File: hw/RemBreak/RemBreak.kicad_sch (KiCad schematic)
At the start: 46 parts, among them IC1 MAX17049G+T10, J1 Conn_01x02, J10 Conn_01x04, J11 Conn_01x01, J3 Conn_01x01, J4 Conn_01x03, J5 Conn_01x02, J6 Conn_01x04, J7 Conn_01x07, J8 Conn_01x03, J9 Conn_01x03, Q1 BC337, Q2 BC337, Q3 BC847, Q4 BC847, U1 L7805, U3 INA219BxDCN, U4 L7805, U5 SeeeduinoXIAO

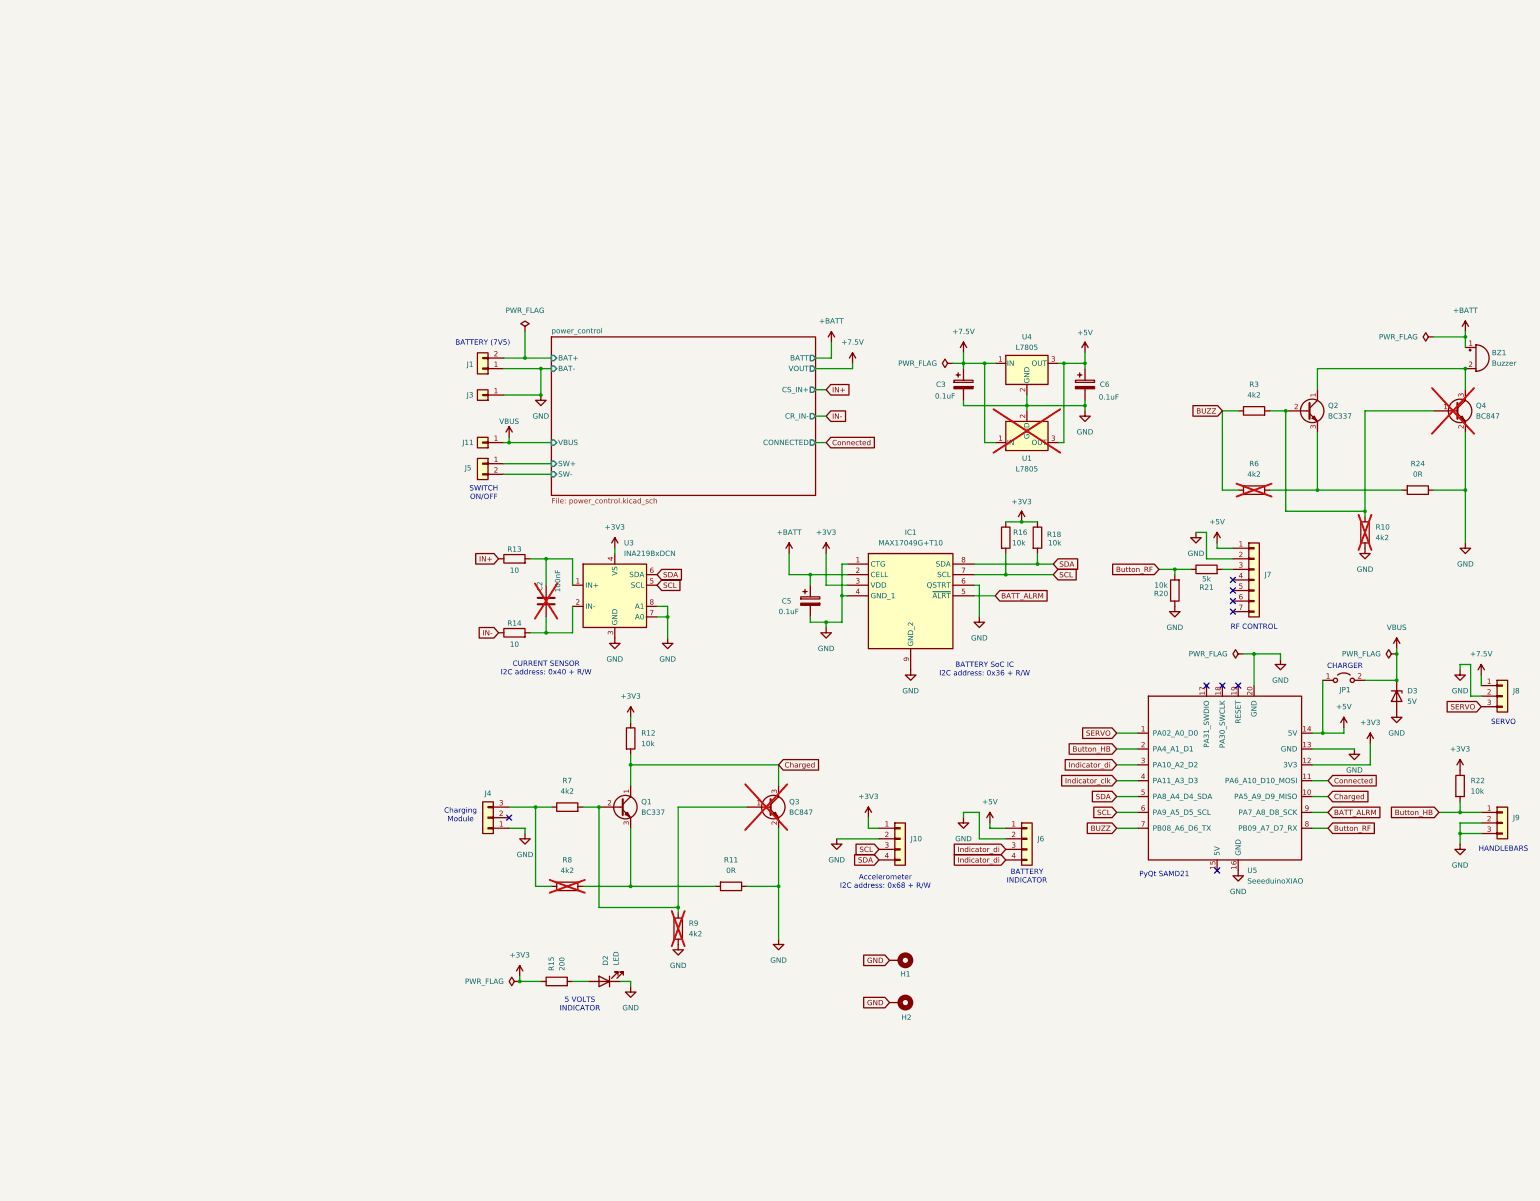
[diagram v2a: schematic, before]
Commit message: updated USBcharger module model
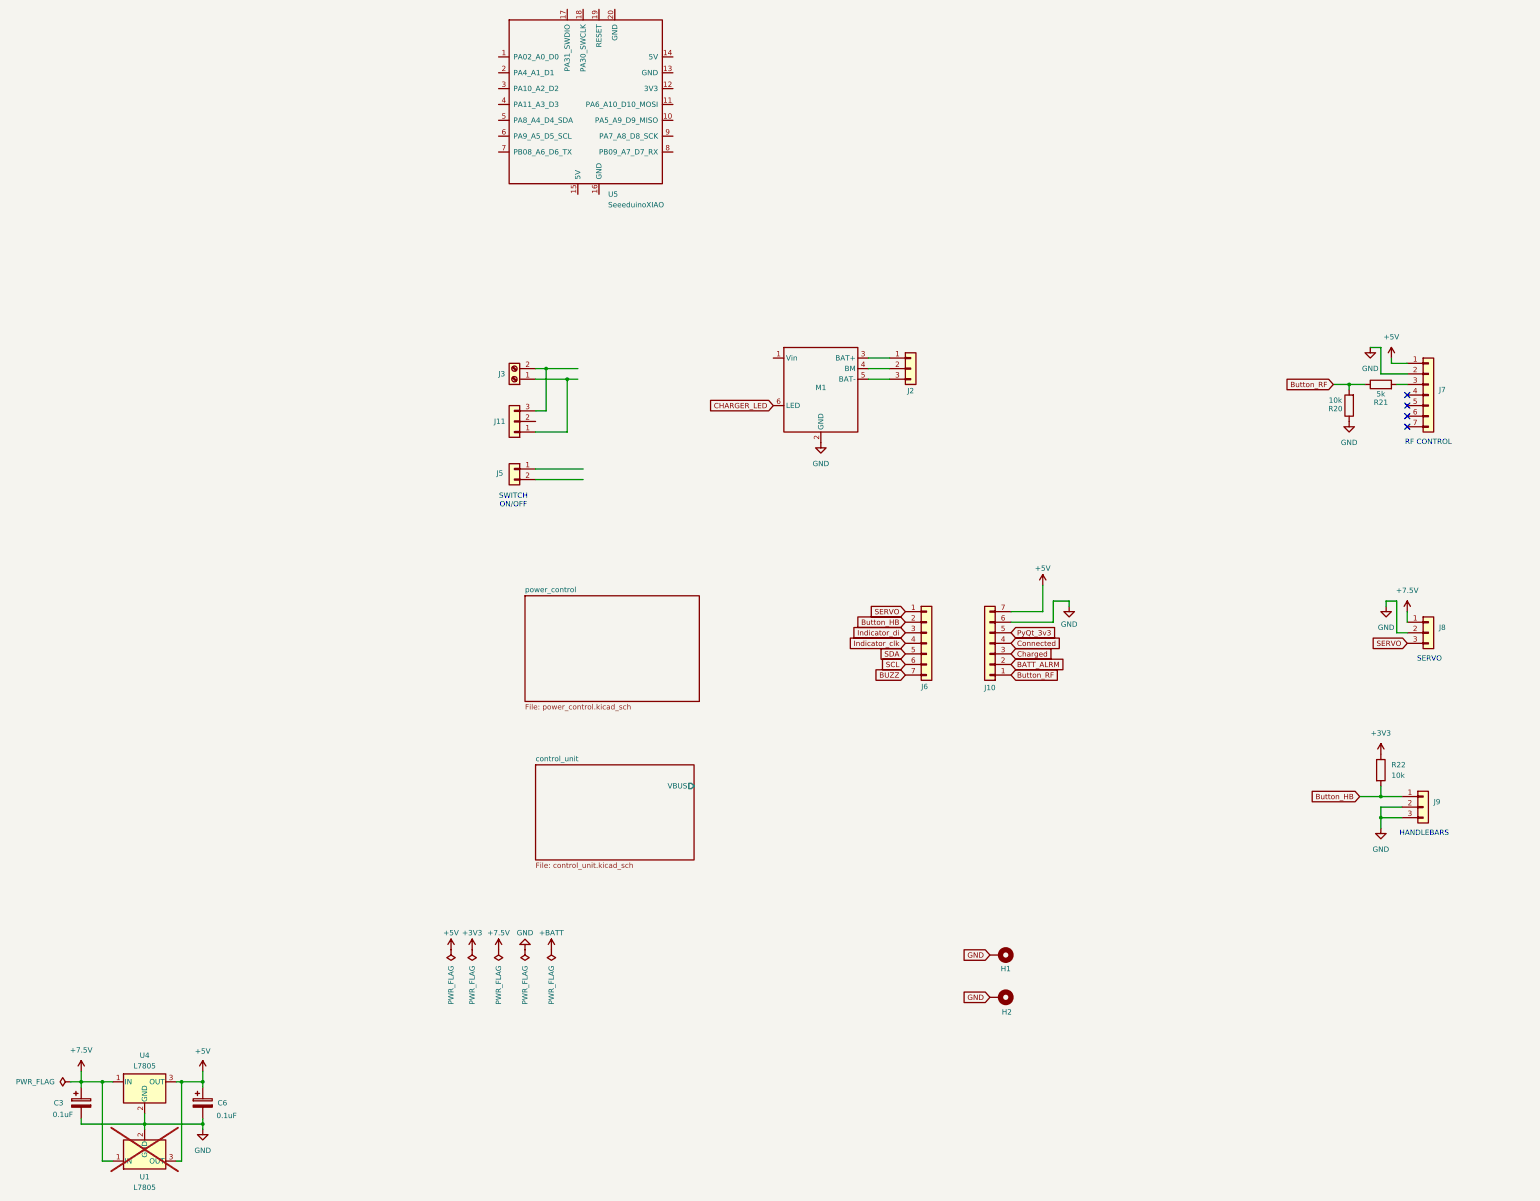
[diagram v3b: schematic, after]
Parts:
- removed BZ1: Buzzer, symbol Device:Buzzer
- removed C2: 100nF, symbol Device:C
- removed C5: 0.1uF, symbol Device:C_Polarized
- removed D2: LED, symbol Device:LED
- removed D3: 5V, symbol Device:D_Zener
- removed IC1: MAX17049G+T10, Package_DFN_QFN:TDFN-8-1EP_2x2mm_P0.5mm_EP0.8x1.2mm, symbol dodo-power:MAX17049G+T10
- removed J1: Conn_01x02, symbol Connector_Generic:Conn_01x02
- removed J10, J6: Conn_01x04, symbol Connector_Generic:Conn_01x04
- removed J11, J3: Conn_01x01, symbol Connector_Generic:Conn_01x01
- removed J4: Conn_01x03, symbol Connector_Generic:Conn_01x03
- removed JP1: Jumper_2_Open, symbol Jumper:Jumper_2_Open
- removed Q1, Q2: BC337, Package_TO_SOT_THT:TO-92_Inline, symbol Transistor_BJT:BC337
- removed Q3, Q4: BC847, Package_TO_SOT_SMD:SOT-23, symbol Transistor_BJT:BC847
- removed R10, R3, R6, R7, R8, R9: 4k2, symbol Device:R
- removed R11, R24: 0R, symbol Device:R
- removed R12, R16, R18: 10k, symbol Device:R
- removed R13, R14: 10, symbol Device:R
- removed R15: 200, symbol Device:R
- removed U3: INA219BxDCN, Package_TO_SOT_SMD:SOT-23-8, symbol Analog_ADC:INA219BxDCN
- added J10, J6: Conn_01x07, symbol Connector_Generic:Conn_01x07
- added J11, J2: Conn_01x03, symbol Connector_Generic:Conn_01x03
- added J3: Screw_Terminal_01x02, symbol Connector:Screw_Terminal_01x02
- added M1: ~, symbol chinese_modules:USBC_charger
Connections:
- net +3V3: no longer U5.12 (3V3)
- net +5V: now also J10.7 (Pin_7); no longer U5.14 (5V)
- net BATT_ALRM: now also J10.2 (Pin_2); no longer U5.9 (PA7_A8_D8_SCK)
- net BUZZ: now also J6.7 (Pin_7); no longer U5.7 (PB08_A6_D6_TX)
- net Button_HB: now also J6.2 (Pin_2); no longer U5.2 (PA4_A1_D1)
- net Button_RF: now also J10.1 (Pin_1); no longer U5.8 (PB09_A7_D7_RX)
- net Charged: now also J10.3 (Pin_3); no longer U5.10 (PA5_A9_D9_MISO)
- net Connected: now also J10.4 (Pin_4); no longer U5.11 (PA6_A10_D10_MOSI)
- net GND: now also J10.6 (Pin_6), M1.2 (GND); no longer U5.13 (GND), U5.16 (GND), U5.20 (GND)
- net Indicator_clk: now also J6.4 (Pin_4); no longer U5.4 (PA11_A3_D3)
- net Indicator_di: now also J6.3 (Pin_3); no longer U5.3 (PA10_A2_D2)
- net SCL: now also J6.6 (Pin_6); no longer U5.6 (PA9_A5_D5_SCL)
- net SDA: now also J6.5 (Pin_5); no longer U5.5 (PA8_A4_D4_SDA)
- net SERVO: now also J6.1 (Pin_1); no longer U5.1 (PA02_A0_D0)
- net power_control/SW+: no longer names the net of J5.1 (Pin_1)
- net power_control/SW-: no longer names the net of J5.2 (Pin_2)
- new net: J2.1 (Pin_1), M1.3 (BAT+)
- new net: J2.2 (Pin_2), M1.4 (BM)
- new net: J2.3 (Pin_3), M1.5 (BAT-)
- new net: J11.1 (Pin_1), J3.1 (Pin_1)
- new net: J11.3 (Pin_3), J3.2 (Pin_2)
- new net CHARGER_LED: M1.6 (LED)
- new net PyQt_3v3: J10.5 (Pin_5)
- no-connect marks 9 -> 4
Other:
- added sheet control_unit (control_unit.kicad_sch)
- sheet power_control ports: added none; removed BAT+, BAT-, BATT, CONNECTED, CR_IN-, CS_IN+, SW+, SW-, VBUS, VOUT
- note removed: "5 VOLTS INDICATOR"
- note removed: "Accelerometer I2C address: 0x68 + R/W"
- note removed: "BATTERY (7V5)"
- note removed: "BATTERY INDICATOR"
- note removed: "BATTERY SoC IC I2C address: 0x36 + R/W"
- note removed: "CHARGER"
- note removed: "CURRENT SENSOR I2C address: 0x40 + R/W"
- note removed: "Charging Module"
- note removed: "PyQt SAMD21"
- moved on the sheet: C3, C6, H1, H2, J5, J7, J8, J9, R20, R21, R22, U1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

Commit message: reorganized subsheets
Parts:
- removed J10, J6, J7: Conn_01x07, symbol Connector_Generic:Conn_01x07
- removed J11, J2, J8, J9: Conn_01x03, symbol Connector_Generic:Conn_01x03
- removed J3: Screw_Terminal_01x02, symbol Connector:Screw_Terminal_01x02
- removed J5: Conn_01x02, symbol Connector_Generic:Conn_01x02
- removed M1: ~, symbol chinese_modules:USBC_charger
- removed R20, R22: 10k, symbol Device:R
- removed R21: 5k, symbol Device:R
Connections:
- no-connect marks 4 -> 0
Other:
- removed sheet control_unit
- removed sheet power_control
- added sheet break_control (break_control.kicad_sch)
- added sheet power_manager (power_manager.kicad_sch)
- added sheet power_switch (power_switch.kicad_sch)
- note removed: "HANDLEBARS"
- note removed: "RF CONTROL"
- note removed: "SERVO"
- note removed: "SWITCH ON/OFF"
- moved on the sheet: U5

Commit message: project update - started drawing the first revision of the board
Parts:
- removed C3, C6: 0.1uF, symbol Device:C_Polarized
- removed U1, U4: L7805, symbol Regulator_Linear:L7805
- removed U5: SeeeduinoXIAO, symbol dodo-device:SeeeduinoXIAO
- added U1: SeeeduinoXIAO, chinese_modules:Seeeduino XIAO-MOUDLE14P-2.54-21X17.8MM, symbol chinese_modules:SeeeduinoXIAO
- H1, H2: footprint (none) -> TestPoint:TestPoint_THTPad_2.0x2.0mm_Drill1.0mm
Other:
- sheet power_manager ports: added 3V3, 5V, BALARM, CHARGING, I2C; removed none

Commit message: schematics drawing in progress
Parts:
- removed U1: SeeeduinoXIAO, chinese_modules:Seeeduino XIAO-MOUDLE14P-2.54-21X17.8MM, symbol chinese_modules:SeeeduinoXIAO
- added J1: Conn_01x03, Connector_PinHeader_2.54mm:PinHeader_1x03_P2.54mm_Vertical_SMD_Pin1Left, symbol Connector_Generic:Conn_01x03
- added J2: Conn_01x04, TerminalBlock_Phoenix:TerminalBlock_Phoenix_MPT-0,5-4-2.54_1x04_P2.54mm_Horizontal, symbol Connector_Generic:Conn_01x04
- added R1, R2, R3: 0R, Resistor_SMD:R_0805_2012Metric, symbol Device:R
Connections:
- net GND: now also J1.2 (Pin_2), J2.2 (Pin_2)
- new net: J2.1 (Pin_1), R2.2
- new net: J2.4 (Pin_4), R2.1, R3.2
- new net break_control/BUTTON: J2.3 (Pin_3)
- new net break_control/BUZZ_pwr: R1.2, R3.1
- new net break_control/PWR: R1.1
- new net break_control/SERVO: J1.3 (Pin_3)
- new net power_switch/SERVO_pwr: J1.1 (Pin_1)
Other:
- sheet break_control ports: added 3V3, BUTTON, BUZZ_pwr, EN, I2C, PWR, SERVO, VBUS; removed none
- sheet power_manager ports: added EN, VBATT, VBUS; removed 5V, BALARM, CHARGING
- sheet power_switch ports: added PWR, PWR_en, SERVO_pwr, VBATT, VBUS; removed none
- note added: "HANDLEBARS + BOOST CONVERTER (12V)"
- note added: "Pro pripad pripojeni neceho na 12-24V, napajeni z externiho DC/DC menice"
- note added: "SERVO"
